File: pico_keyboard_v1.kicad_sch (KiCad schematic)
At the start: 15 parts, among them J1 Conn_01x04_12864, J2 Conn_01x03_Female, J3 Conn_01x03_Female, SW1 RotaryEncoder_Switch, U1 COM-09032, U2 Pico

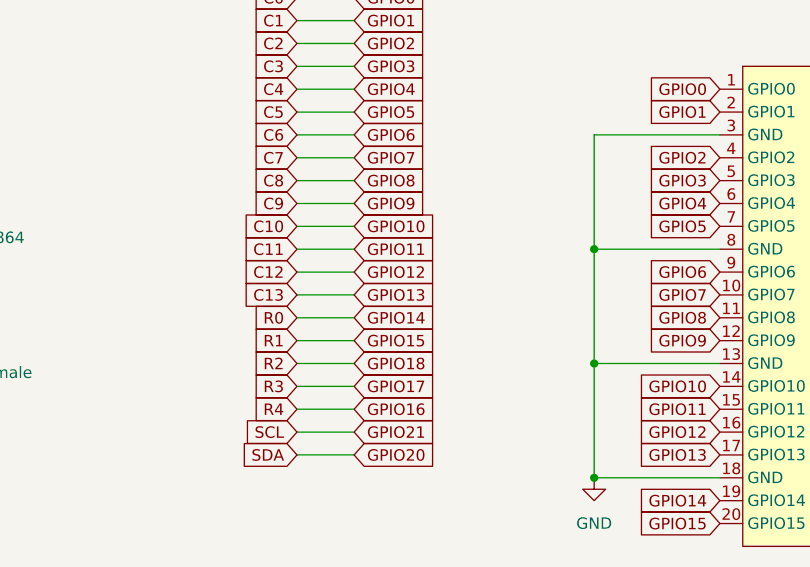
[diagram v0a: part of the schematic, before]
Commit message: Changed layout a bit. Starting of V0.4
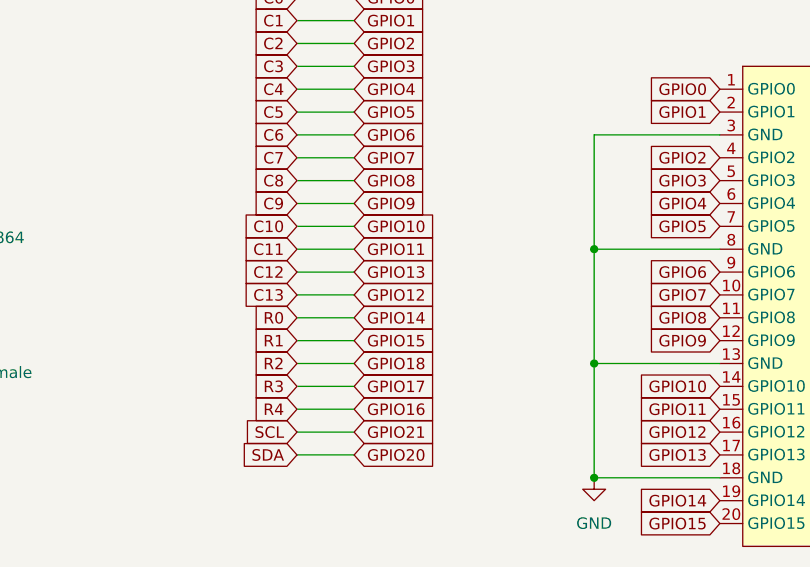
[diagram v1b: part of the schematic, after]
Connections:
- net C12: now also U2.17 (GPIO13); no longer U2.16 (GPIO12)
- net C13: now also U2.16 (GPIO12); no longer U2.17 (GPIO13)
